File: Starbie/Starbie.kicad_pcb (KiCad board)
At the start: 2 copper layers, 119.5 x 84.5 mm, 7 parts, among them J1 Conn_01x04_Pin, J2 Conn_01x08_Pin, SW1 SW_Push, SW2 SW_Push, U1 XIAO-ESP32-C3-SMD, U2 DHT11

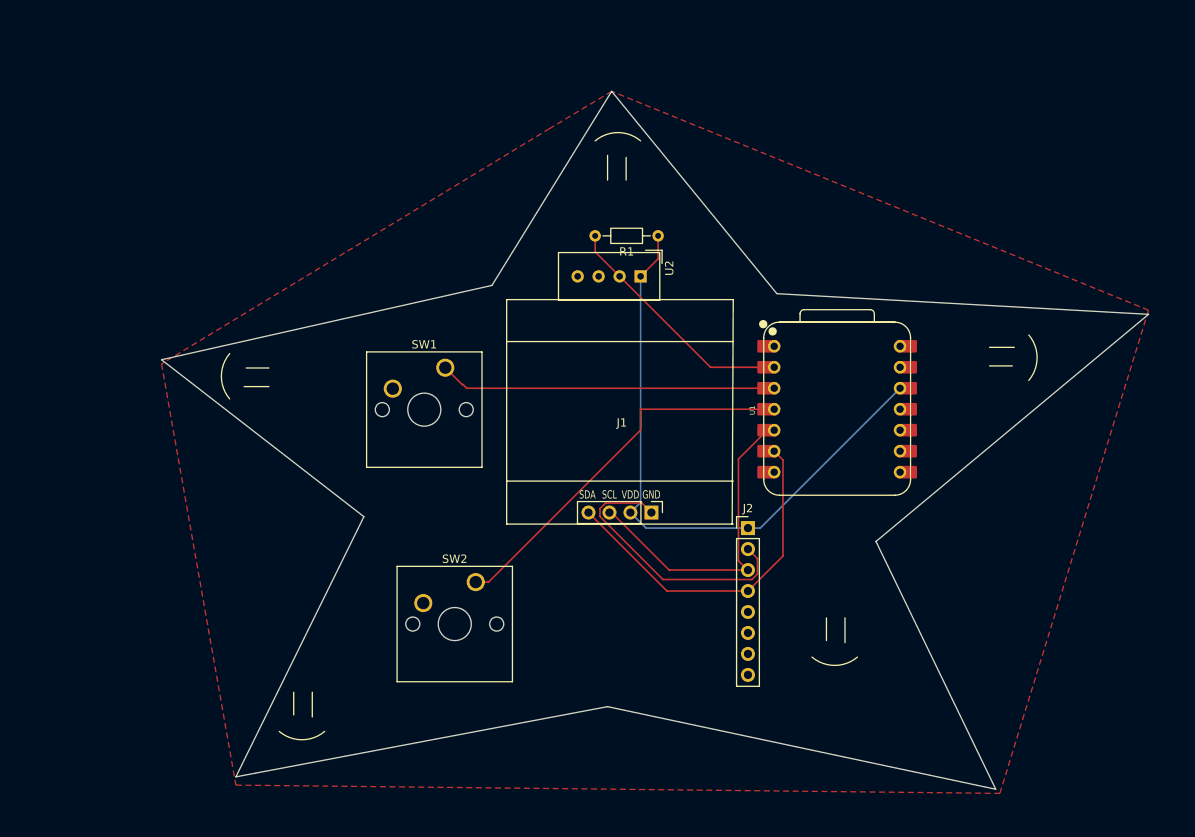
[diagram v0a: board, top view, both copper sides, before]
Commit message: add switch, LED mood lighting and battery connectors (and testpoint also) + routed everything + rounded star edges
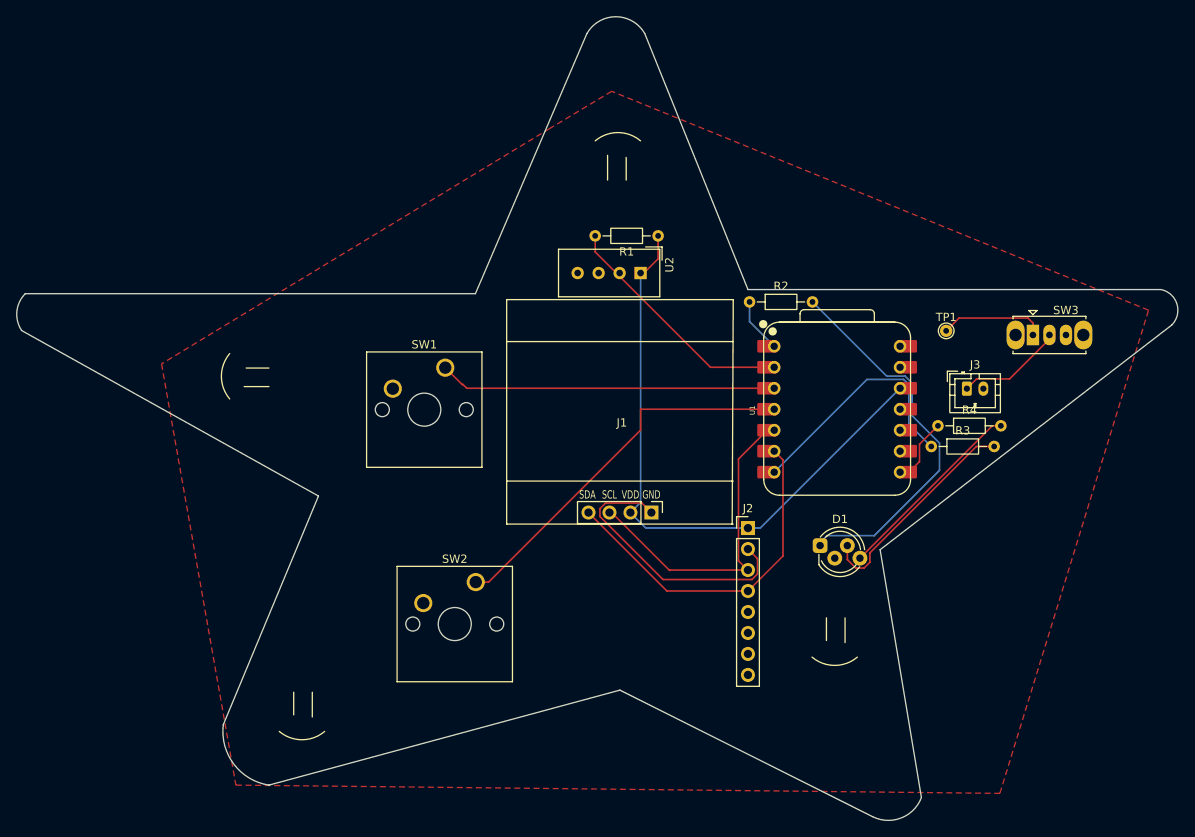
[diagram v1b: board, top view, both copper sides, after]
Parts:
- added D1: LED_RKGB, LED_THT:LED_D5.0mm-4_RGB_Staggered_Pins, F.Cu at (156.2, 104.0)
- added J3: Conn_01x02_Socket, Connector_JST:JST_PH_B2B-PH-K_1x02_P2.00mm_Vertical, F.Cu at (174.0, 85.0)
- added R2: 220, Resistor_THT:R_Axial_DIN0204_L3.6mm_D1.6mm_P7.62mm_Horizontal, F.Cu at (147.7, 74.5)
- added R3: 220, Resistor_THT:R_Axial_DIN0204_L3.6mm_D1.6mm_P7.62mm_Horizontal, F.Cu at (169.7, 92.0)
- added R4: 220, Resistor_THT:R_Axial_DIN0204_L3.6mm_D1.6mm_P7.62mm_Horizontal, F.Cu at (170.5, 89.5)
- added SW3: SW_SPDT, Button_Switch_THT:SW_Slide_SPDT_Straight_CK_OS102011MS2Q, F.Cu at (182.0, 78.5)
- added TP1: TestPoint, TestPoint:TestPoint_THTPad_D1.5mm_Drill0.7mm, F.Cu at (171.5, 78.0)
- moved U2 0.40 mm to (134.5, 71.0)
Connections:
- U1 pad 1: unconnected-(U1-D0-Pad1)_1 -> /LED_R
- U1 pad 7: unconnected-(U1-D6-Pad7) -> /LED_G
- U1 pad 8: unconnected-(U1-D7-Pad8)_1 -> /LED_B
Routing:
- net Net-(D1-RA): track 0.00 -> 46.5 mm
- net /LED_G: track 0.00 -> 29.8 mm
- net Net-(D1-GA): track 0.00 -> 26.9 mm
- net Net-(D1-BA): track 0.00 -> 23.7 mm
- net /BAT_RAW: track 0.00 -> 13.0 mm
- net /VBAT_SW: track 0.00 -> 12.8 mm
- net /LED_B: track 0.00 -> 8.14 mm
- net /LED_R: track 0.00 -> 6.61 mm
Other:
- board size 119.5 x 84.5 mm -> 140.6 x 97.3 mm

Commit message: fixing porting error in pcb + schematic, start firmware and program led functionality
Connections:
- U1 pad 1: /LED_R -> unconnected-(U1-D0-Pad1)_1
- U1 pad 11: unconnected-(U1-D10-Pad11) -> /LED_R
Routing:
- net /LED_R: track 6.61 -> 23.6 mm

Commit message: label
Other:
- board text added: "+"
- board text added: "-"
- board text added: "Menu"
- board text added: "OFF"
- board text added: "ON"
- board text added: "Starbie v1 by Vincent"
- board text added: "Stats"
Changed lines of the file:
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@@
 		(layer "Edge.Cuts")
+	)
+	(gr_text "Menu"
+		(at 97.5 92.5 90)
+		(layer "F.SilkS")
+		(effects
+			(font
+				(size 3 3)
+				(thickness 0.1)
+			)
+			(justify left bottom)
+		)
+	)
+	(gr_text "Stats"
+		(at 101 119 90)
+		(layer "F.SilkS")
+		(effects
+			(font
+				(size 3 3)
+				(thickness 0.1)
+			)
+			(justify left bottom)
+		)
+	)
+	(gr_text "+\n"
+		(at 171.5 85.5 0)
+		(layer "B.SilkS")
+		(effects
+			(font
+				(size 1 1)
+				(thickness 0.1)
+			)
+			(justify left bottom mirror)
+		)
+	)
+	(gr_text "ON"
+		(at 178 79 0)
+		(layer "B.SilkS")
+		(effects
+			(font
+				(size 1 1)
+				(thickness 0.1)
+			)
+			(justify left bottom mirror)
+		)
+	)
+	(gr_text "-\n"
+		(at 180 85.5 0)
+		(layer "B.SilkS")
+		(effects
+			(font
+				(size 1 1)
+				(thickness 0.1)
+			)
+			(justify left bottom mirror)
+		)
+	)
+	(gr_text "OFF"
+		(at 192.5 79 0)
+		(layer "B.SilkS")
+		(effects
+			(font
+				(size 1 1)
+				(thickness 0.1)
+			)
+			(justify left bottom mirror)
+		)
+	)
+	(gr_text "Starbie v1\nby Vincent"
+		(at 165 129 0)
+		(layer "B.SilkS")
+		(effects
+			(font
+				(size 2 2)
+				(thickness 0.3)
+			)
+			(justify left bottom mirror)
+		)
 	)
 	(segment

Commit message: decor
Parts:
- added ?: LOGO, Imported_Parts:gh_qr, F.Cu at (86.0, 81.0)
- added ?: LOGO, Imported_Parts:star_silkscreen, F.Cu at (131.0, 49.5)
- added ?: LOGO, Imported_Parts:uplook, F.Cu at (131.0, 110.5)
- added ?: LOGO, Imported_Parts:star_silkscreen, B.Cu at (131.0, 49.5)
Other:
- board text added: "USB"
- board text added: "zZzZz"
- board text added: "❤"
